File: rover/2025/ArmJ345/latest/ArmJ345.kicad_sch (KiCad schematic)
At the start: 4 parts

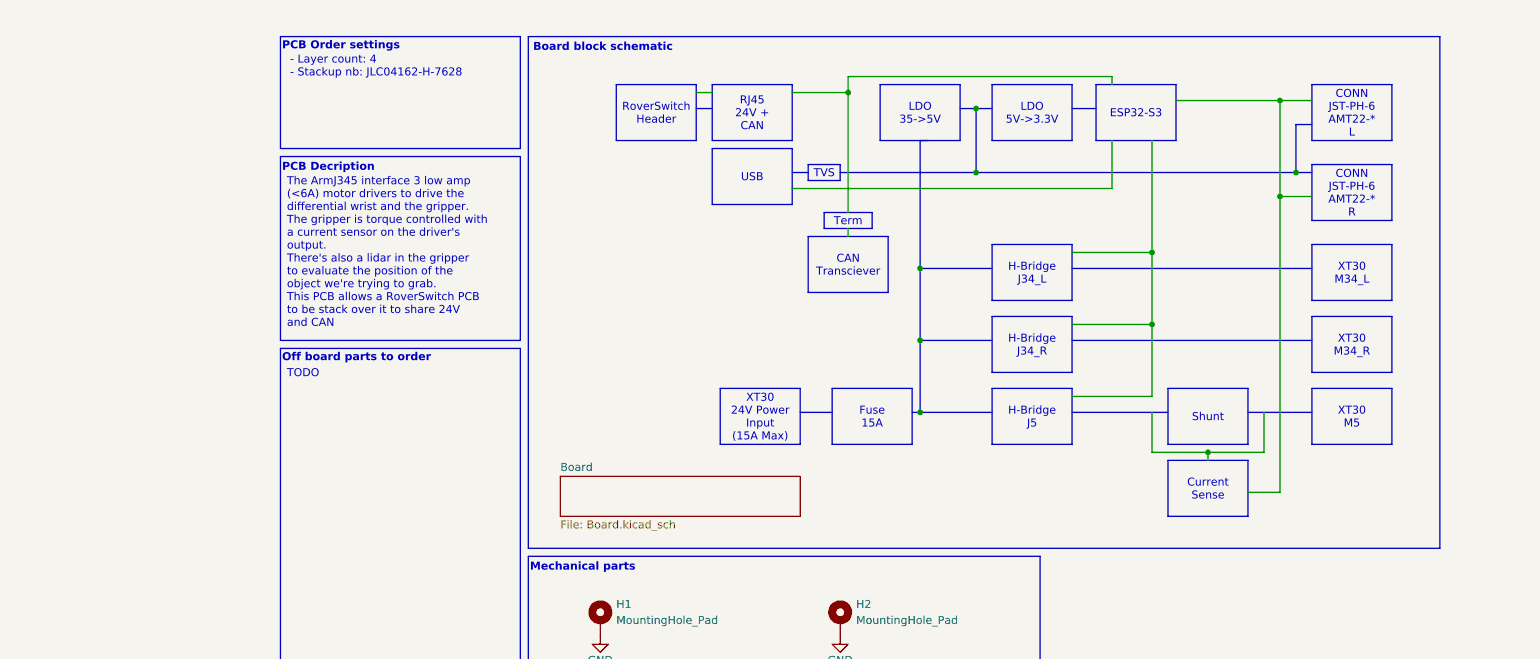
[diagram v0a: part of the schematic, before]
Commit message: ArmJ345 routing
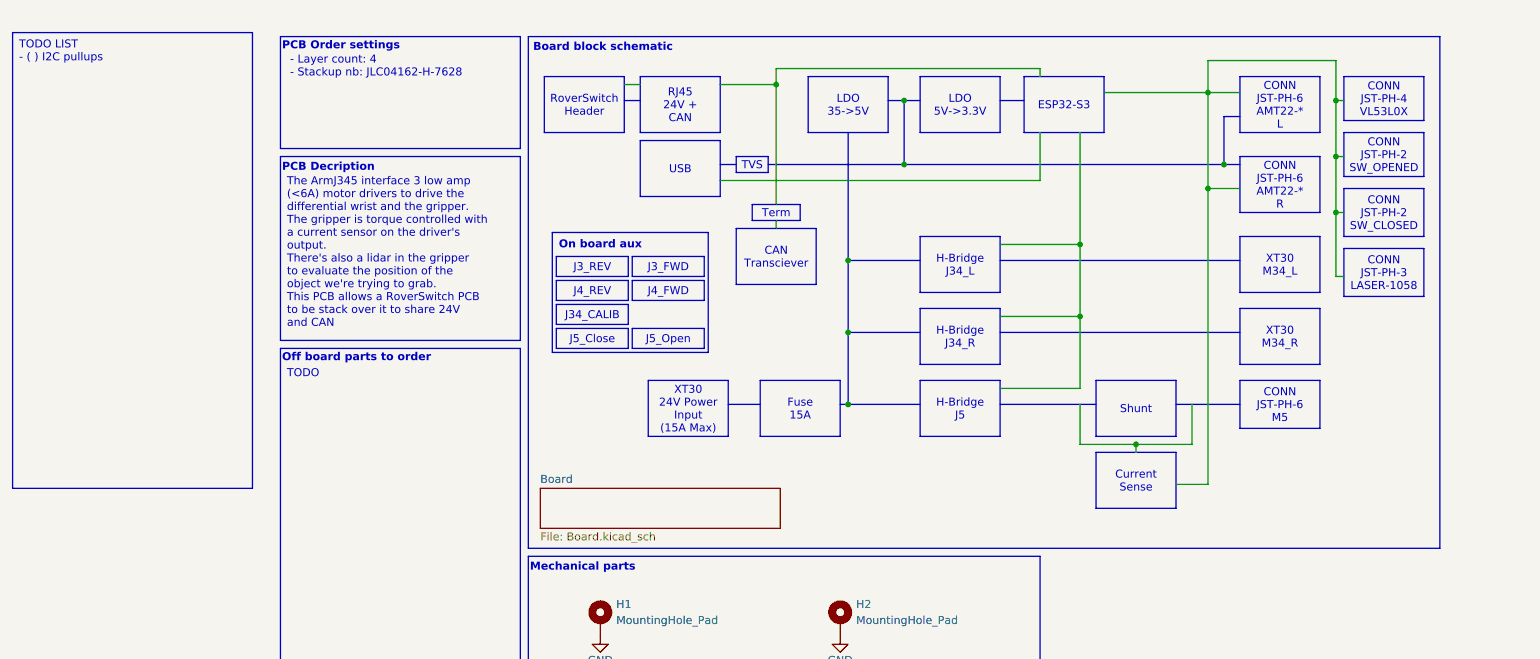
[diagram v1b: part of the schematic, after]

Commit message: Done
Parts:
- added G1: ST0242, symbol RoverLibrary:Off Board Part
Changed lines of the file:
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@@
-		)
-	)
-	(text_box "TODO LIST\n  - ( ) I2C pullups"
-		(exclude_from_sim no)
-		(at -29.845 12.065 0)
-		(size 38.1 72.39)
-		(stroke
-			(width 0)
-			(type default)
-		)
-		(fill
-			(type none)
-		)
-		(effects
-			(font
-				(size 1.27 1.27)
-			)
-			(justify left top)
 		)
 	)
@@
 					(unit 1)
 				)
+			)
+		)
+	)
+	(symbol
+		(lib_id "RoverLibrary:Off Board Part")
+		(at 24.13 72.39 0)
+		(unit 1)
+		(exclude_from_sim yes)
+		(in_bom yes)
+		(on_board no)
+		(dnp no)
+		(fields_autoplaced yes)
+		(property "Reference" "G1"
+			(at 24.13 30.5501 0)
+			(effects
+				(font
+					(size 1.27 1.27)
+				)
+				(hide yes)
+			)
+		)
+		(property "Value" "ST0242"
+			(at 24.13 72.39 0)
+			(do_not_autoplace yes)
+			(effects
+				(font
+					(size 1.27 1.27)
+				)
+			)
+		)
+		(property "Footprint" ""
+			(at 21.59 71.12 0)
+			(effects
+				(font
+					(size 1.27 1.27)
+				)
+				(hide yes)
+			)
+		)
+		(property "Datasheet" "https://www.sunfounder.com/products/vl53l0x-time-of-flight-distance-sensor-laser-ranging-module"
+			(at 21.59 71.12 0)
+			(effects
+				(font
+					(size 1.27 1.27)
+				)
+				(hide yes)
+			)
+		)
+		(property "Description" ""
+			(at 21.59 71.12 0)
+			(effects
+				(font
+					(size 1.27 1.27)
+				)
+				(hide yes)
+			)
+		)
+		(instances
+			(project ""
+				(path "/a4fa9b30-7b48-474a-bdaa-0d7a6d26a697"
+					(reference "G1")
+					(unit 1)
+				)

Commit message: J345 Fix
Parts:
- added G10: 1528-1403-ND, symbol RoverLibrary:Off Board Part
- added G2: JUMPER 2PINS (QPC02SXGN-RC), symbol RoverLibrary:Off Board Part
- added G3, G4: PHR-2, symbol RoverLibrary:Off Board Part
- added G5: PHR-3, symbol RoverLibrary:Off Board Part
- added G6: PHR-4, symbol RoverLibrary:Off Board Part
- added G7, G8, G9: PHR-6, symbol RoverLibrary:Off Board Part

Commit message: PCBs ordered
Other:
- note added: "- Layer count: 4 - Stackup nb: JLC04161-H-7628"
- note removed: "- Layer count: 4 - Stackup nb: JLC04162-H-7628"
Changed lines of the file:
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@@
 		)
 	)
-	(text "- Layer count: 4\n- Stackup nb: JLC04162-H-7628\n"
+	(text "- Layer count: 4\n- Stackup nb: JLC04161-H-7628\n"
 		(exclude_from_sim no)
 		(at 14.224 15.748 0)

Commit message: .
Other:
- note removed: "0.2A Trace"
- note removed: "12.2A Trace"
- note removed: "15A Trace"
- note removed: "2A Trace"
- note removed: "4A Trace"
